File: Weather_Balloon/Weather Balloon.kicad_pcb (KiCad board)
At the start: 2 copper layers, 182.4 x 96.5 mm, 197 parts, among them IC1 ATTINY85-P, IC2 ATMEGA2560-A, M1 MountingHole_2.5mm, M2 MountingHole_2.5mm, M3 MountingHole_2.5mm, M4 MountingHole_2.5mm, P1 85_PRGM, P10 SERIAL, P12 Custom_HEAT, P13 SHT31_HEAT, P14 GPS_HEAT, P15 UV_HEAT, P16 TSL2561_HEAT, P17 LSM9DS1, P18 PIEZO, P19 MICRO_SD_CARD, P20 LANDING_LED, P21 DS18B20, P22 RADIO, P23 EXT_SENSORS, P26 MS5607, P27 GPS, P28 5V_BOOST, P4 2560_RESET, P5 2560_SCK, P6 2560_MOSI, P7 2560_MISO, P8 85_RESET, P9 Geiger, Q1 PSMN9R1-30YL,115, Q10 PSMN9R1-30YL,115, Q11 PSMN9R1-30YL,115, Q12 PSMN9R1-30YL,115, Q13 PSMN9R1-30YL,115, Q14 PSMN9R1-30YL,115, Q15 PSMN9R1-30YL,115, Q16 PSMN9R1-30YL,115, Q17 PSMN9R1-30YL,115, Q2 PSMN9R1-30YL,115, Q3 PSMN9R1-30YL,115, Q4 PSMN9R1-30YL,115, Q5 PSMN9R1-30YL,115, Q6 PSMN9R1-30YL,115, Q7 PSMN9R1-30YL,115, Q8 PSMN9R1-30YL,115, Q9 PSMN9R1-30YL,115, SW1 SILENCE, U1 MAX6107EUR, U10 AT25_EEPROM, U11 AT25_EEPROM, U12 AT25_EEPROM, U13 AT25_EEPROM, U14 AT25_EEPROM, U15 AT25_EEPROM, U16 LD1117S33TR, U2 BILEVEL_SHIFT, U3 BILEVEL_SHIFT, U4 DS3231, U5 FUEL_GAUGE, U6 AT25_EEPROM, U7 AT25_EEPROM, U8 AT25_EEPROM, U9 AT25_EEPROM, Y1 16Mhz

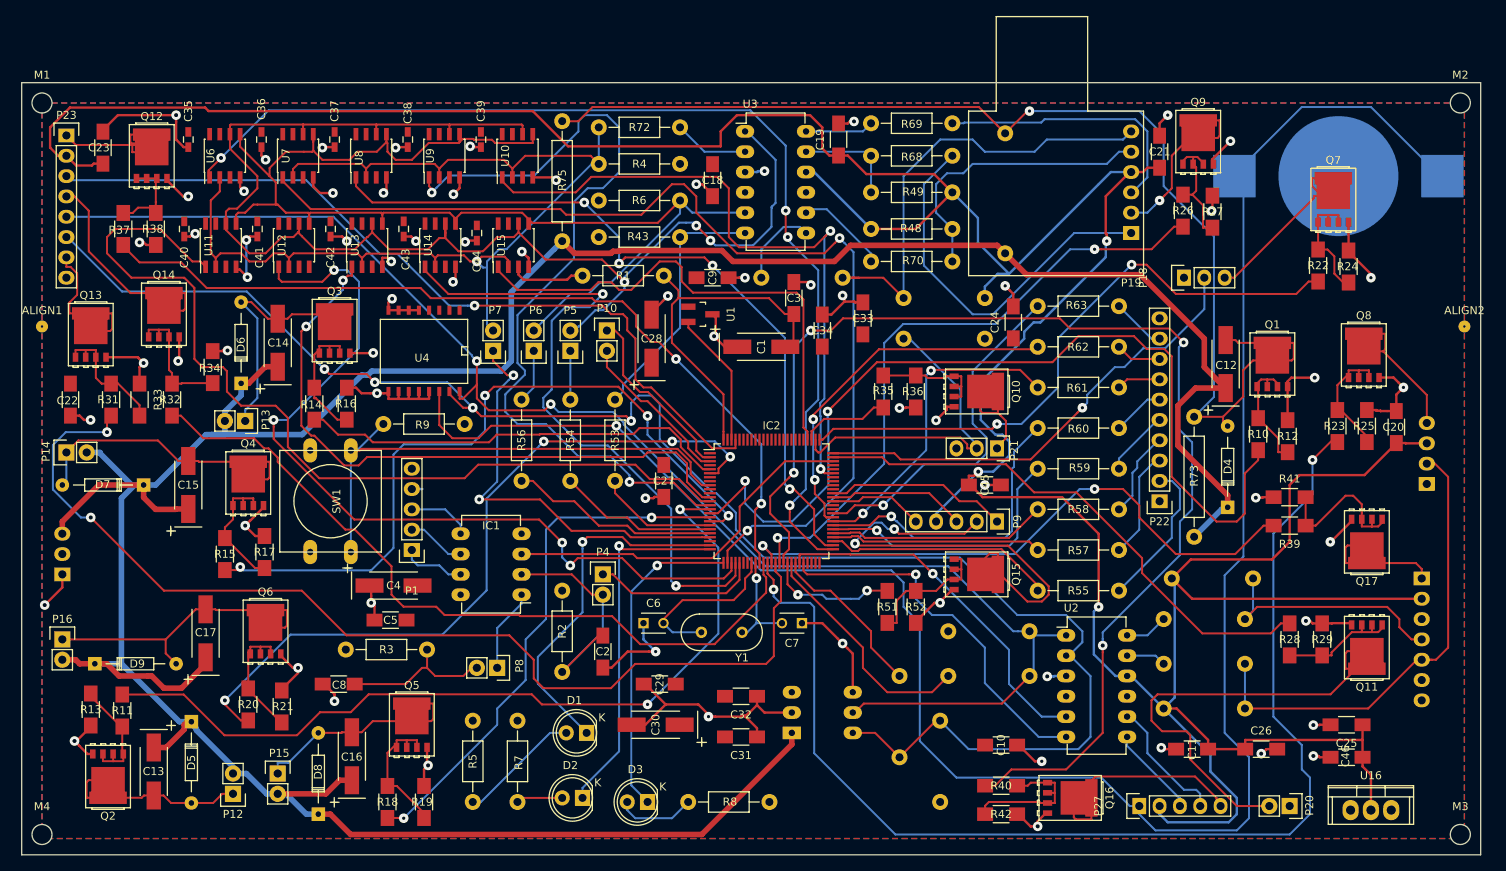
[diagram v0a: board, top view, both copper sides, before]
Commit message: Before manual trace width adjust
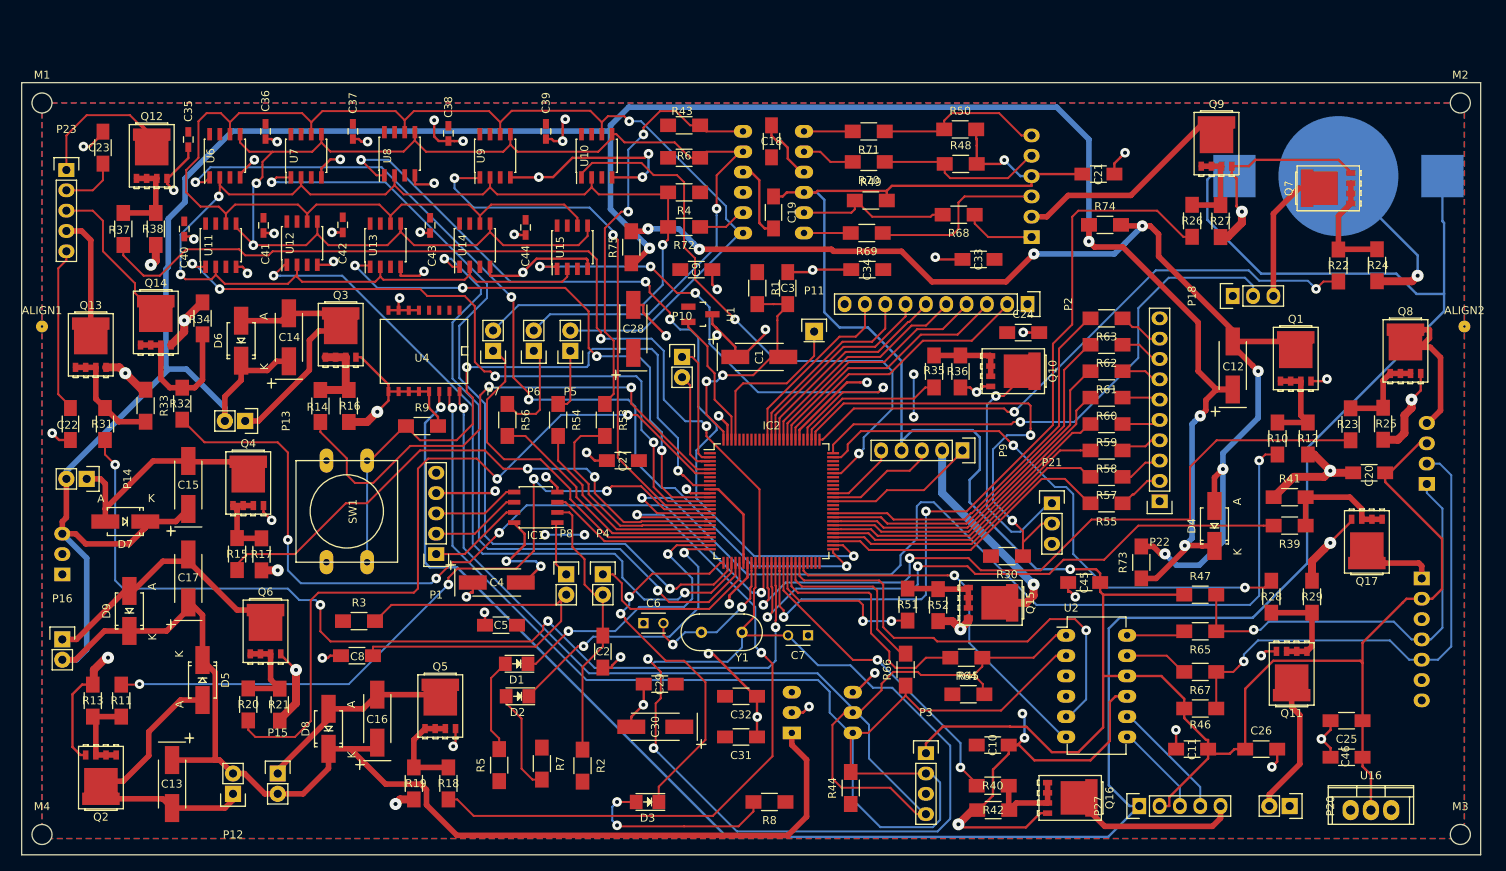
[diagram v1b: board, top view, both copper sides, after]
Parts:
- added P11: UV_ADC, Pin_Headers:Pin_Header_Straight_1x01, F.Cu at (156.2, 78.9)
- added P2: ADC_AUX, Pin_Headers:Pin_Header_Straight_1x10, F.Cu at (182.9, 75.4)
- added P3: SENSOR_I2C, Pin_Headers:Pin_Header_Straight_1x04, F.Cu at (170.2, 131.6)
- D1, D2, D3: footprint LEDs:LED-5MM -> LEDs:LED_1206
- D4, D5, D6, D7, D8, D9: footprint Diodes_ThroughHole:Diode_DO-35_SOD27_Horizontal_RM10 -> Diodes_SMD:SMA_Handsoldering
- IC1: footprint Housings_DIP:DIP-8_W7.62mm_LongPads -> Housings_SOIC:SOIC-8_3.9x4.9mm_Pitch1.27mm
- P1, P27, P9: footprint Personal:Pin_Header_Straight_1x05_Double_Sided -> Pin_Headers:Pin_Header_Straight_1x05
- P10, P12, P13, P14, P15, P16, P20, P4, P5, P6, P7, P8: footprint Personal:Pin_Header_Straight_1x02 -> Pin_Headers:Pin_Header_Straight_1x02
- P17: footprint Personal:LSM9DS1_BACK -> Personal:LSM9DS1_ALL
- P19: footprint Personal:MicroSD_BACK -> Personal:MicroSD_ALL; moved to B.Cu
- P21: footprint Personal:Pin_Header_Straight_1x03_ALL -> Pin_Headers:Pin_Header_Straight_1x03
- P23: footprint Pin_Headers:Pin_Header_Straight_1x08 -> Pin_Headers:Pin_Header_Straight_1x05
- P26: footprint Personal:MS5607_BACK -> Personal:MS5607_ALL
- P28: footprint Personal:Voltage_Booster_BACK -> Personal:Voltage_Booster_ALL
- R1, R2, R3, R4, R43, R48, R49, R5, R53, R54, R55, R56, R57, R58, R59, R6, R60, R61, R62, R63, R68, R69, R7, R70, R72, R8, R9: footprint Resistors_ThroughHole:Resistor_Horizontal_RM10mm -> Resistors_SMD:R_1206_HandSoldering
- R30, R44, R45, R46, R47, R50, R64, R65, R66, R67, R71: footprint Resistors_ThroughHole:Resistor_Horizontal_RM10mm -> Resistors_SMD:R_1206_HandSoldering; moved to F.Cu
- R73, R75: footprint Resistors_ThroughHole:Resistor_Horizontal_RM15mm -> Resistors_SMD:R_1206_HandSoldering
- R74: footprint Resistors_ThroughHole:Resistor_Horizontal_RM15mm -> Resistors_SMD:R_1206_HandSoldering; moved to F.Cu
- U2: footprint Personal:DIP-12_W7.62mm_LongPads_BACK -> Personal:DIP-12_W7.62mm_LongPads_ALL
- U3: footprint Personal:DIP-12_W7.62mm_LongPads_BACK -> Personal:DIP-12_W7.62mm_LongPads_ALL; moved to B.Cu
- U5: footprint Personal:FUEL_GAUGE_BACK -> Personal:FUEL_GAUGE_ALL
- Y1: footprint Personal:HC-49V -> Crystals:HC-49V
- moved R30 30.1 mm to (180.3, 106.9), turned to 180 degrees
- moved R50 22.2 mm to (174.5, 53.6)
- moved R1 21.9 mm to (149.1, 73.4), turned to 270 degrees
- moved R71 18.6 mm to (163.0, 53.8)
- moved R43 17.6 mm to (140.0, 53.1)
- moved C45 17.4 mm to (190.0, 110.2), turned to 0 degrees
- moved R69 17.4 mm to (162.8, 66.5)
- moved R70 16.2 mm to (163.0, 57.7)
- moved C33 16.2 mm to (176.8, 69.8), turned to 180 degrees
- moved D2 15.1 mm to (119.1, 124.5)
- moved P8 14.5 mm to (125.2, 109.2), turned to 0 degrees
- moved C5 13.8 mm to (117.1, 115.6)
- moved R74 13.0 mm to (192.6, 65.5), turned to 0 degrees
- moved C4 12.9 mm to (116.5, 110.2)
- moved U3 12.7 mm to (147.3, 66.5)
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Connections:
- C22 pad 1: Vcc_1 -> Net-(C22-Pad1)
- C23 pad 1: +3V3 -> Net-(C23-Pad1)
- IC2 pad 23: (no net) -> 2560_HEARTBEAT
- IC2 pad 73: 2560_HEARTBEAT -> (no net)
- IC2 pad 82: (no net) -> Net-(IC2-Pad82)
- IC2 pad 83: (no net) -> Net-(IC2-Pad83)
- IC2 pad 84: (no net) -> Net-(IC2-Pad84)
- IC2 pad 85: (no net) -> Net-(IC2-Pad85)
- IC2 pad 86: (no net) -> Net-(IC2-Pad86)
- IC2 pad 87: (no net) -> Net-(IC2-Pad87)
- IC2 pad 88: (no net) -> Net-(IC2-Pad88)
- IC2 pad 89: (no net) -> Net-(IC2-Pad89)
- P23 pad 2: +3V3 -> Net-(C23-Pad1)
- P23 pad 3: UV_VOLTAGE -> SHT_31_PWR
- P23 pad 4: SHT_31_PWR -> Net-(P23-Pad4)
- P23 pad 5: SCL_5 -> Net-(C22-Pad1)
- P9 pad 1: GEIGER_Z -> GEIGER_X
- P9 pad 5: GEIGER_X -> GEIGER_Z
- Q13 pad 2: Net-(P23-Pad7) -> Net-(P23-Pad4)
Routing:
- net +3V3: track 468.6 -> 307.7 mm, vias 3 -> 2
- net GND: track 308.4 -> 467.9 mm, vias 66 -> 75
- net GPS_POWER: track 152.7 -> 39.7 mm, vias 4 -> 2
- net Net-(C7-Pad2): track 13.1 -> 119.4 mm, vias 1 -> 2
- net UV_VOLTAGE: track 102.7 -> 20.8 mm, vias 1 -> 0
- net +BATT: track 400.0 -> 479.0 mm, vias 0 -> 4
- net DOF_POWER: track 148.4 -> 94.0 mm
- net SDA_5: track 210.5 -> 157.3 mm, vias 4 -> 1
- net MISO: track 135.4 -> 175.5 mm, vias 1 -> 3
- net Net-(P20-Pad2): track 58.1 -> 18.1 mm
- net Net-(P19-Pad1): track 47.8 -> 8.91 mm
- net SS_3.3: track 58.2 -> 21.1 mm
- net AT25_CS_7: track 105.1 -> 69.1 mm
- net Net-(C8-Pad1): track 19.2 -> 53.9 mm
- net Net-(IC2-Pad82): track 0.00 -> 34.5 mm
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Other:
- net class Default: clearance 0.2 -> 0.01
- net class Heat: clearance 0.3 -> 0.01
- net class Power: clearance 0.2 -> 0.01
- rule trace_clearance: 0.2 -> 0.01
